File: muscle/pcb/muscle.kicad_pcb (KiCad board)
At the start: 4 copper layers, 135 x 50 mm, 166 parts, among them J1 B4B-XH-2(LF)(SN), J10 USB4115-03-C, J2 WAFER-SH1.0-3PWB, J4 WAFER-SH1.0-3PWB, J5 B4B-XH-2(LF)(SN), J8 B2B-XH-A(LF)(SN), J9 USB4115-03-C, Q1 AO3401A, Q10 BSS138W, Q2 AONR21321, Q3 WSD6070DN56, Q4 WSD6070DN56, Q5 BSS138W, Q6 WSD6070DN56, Q7 AONR21321, Q8 WSD6070DN56, Q9 AGM18N10AP, SW1 TS3425BA, SW2 TS3425BA, U1 TMC2209-LA, U10 TPS62933, U13 TLV75733PDBV, U14 DRV8701P, U2 TMC2209-LA, U3 RP2350A, U4 CYPD3177-24LQ, U5 LM5156, U6 W25Q128JVSS, Y1 ABM8-272-T3

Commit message: muscle: more TMC air
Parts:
- RV4: value I_{SINK_COARSE} -> I_{SNK_COARSE}
- moved RV4 0.50 mm to (111.0, 118.2)
- moved C32 0.35 mm to (141.4, 117.2)
- moved C23 0.23 mm to (77.3, 103.4)
- moved RV6 0.10 mm to (107.7, 100.9)
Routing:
- net /Y_DIR: track 130.5 -> 126.5 mm
- net /X_DIR: track 84.0 -> 81.0 mm
- net +3V3: track 150.3 -> 152.4 mm, vias 4 -> 6
- net /STEP_UART: track 117.8 -> 119.7 mm
- net /X_STEP: track 77.7 -> 79.5 mm
- net GND: track 149.2 -> 150.9 mm
- net /PD_VDDD: track 28.8 -> 30.5 mm
- net /Y_STEP: track 120.8 -> 119.3 mm
- net Net-(U1-VREF): track 9.07 -> 10.5 mm
- net /~{DRV_EN}: track 132.1 -> 131.1 mm
- net /X_DIAG: track 76.2 -> 76.8 mm
- net /Y_DIAG: track 112.5 -> 111.9 mm
- net /ISNK_COARSE: track 5.91 -> 6.41 mm

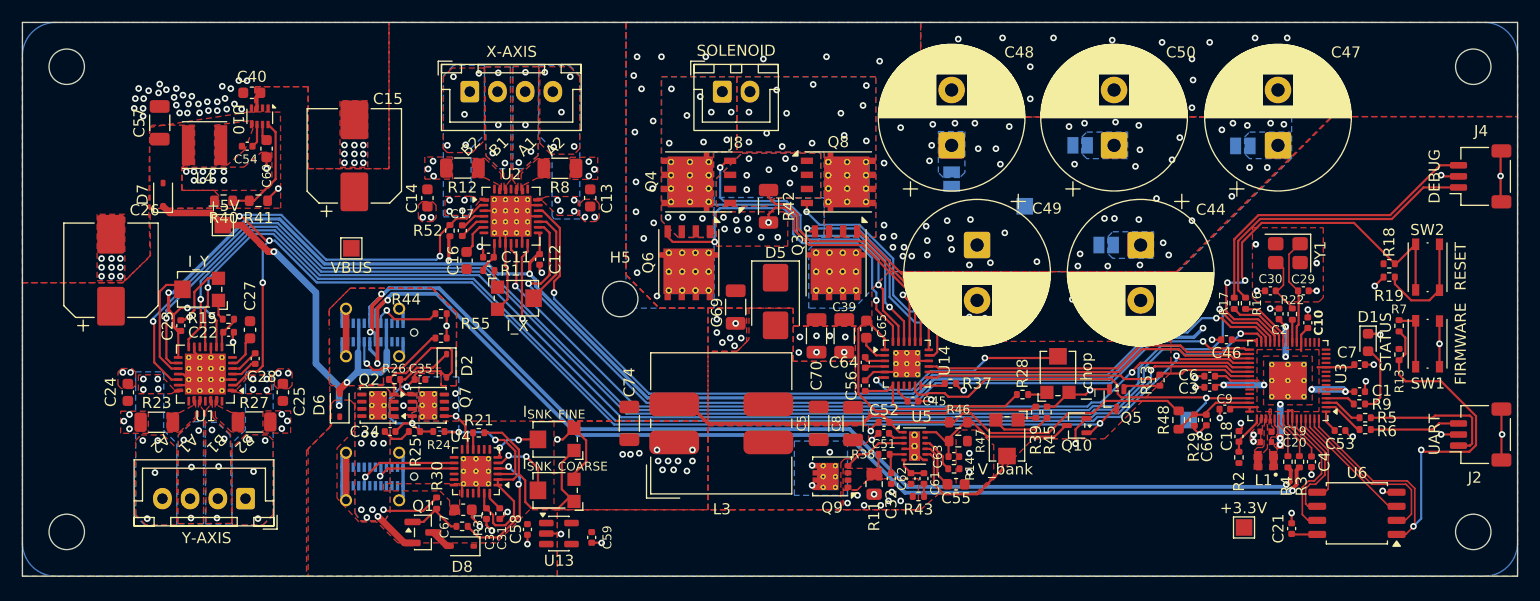
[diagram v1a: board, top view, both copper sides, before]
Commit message: muscle: tweak for easier USB-C flipping
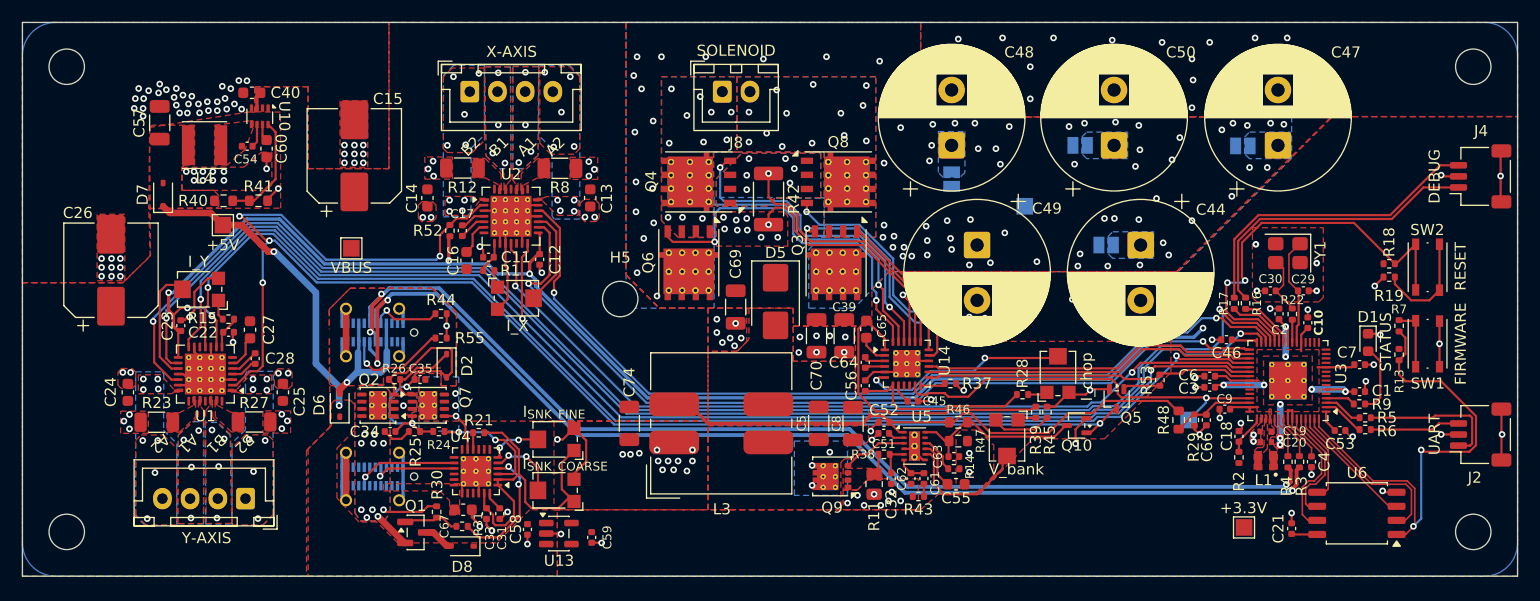
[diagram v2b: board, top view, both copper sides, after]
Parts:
- R42: footprint Resistor_SMD:R_1206_3216Metric -> Resistor_SMD:R_2010_5025Metric
- moved R30 0.80 mm to (100.4, 120.2)
- moved Q1 0.66 mm to (98.5, 122.0)
- moved R42 0.65 mm to (130.4, 92.0)
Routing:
- net Net-(U14-SP): track 23.6 -> 25.1 mm
- net VBUS0: track 12.2 -> 11.3 mm
- net Net-(D8-A): track 2.05 -> 2.71 mm

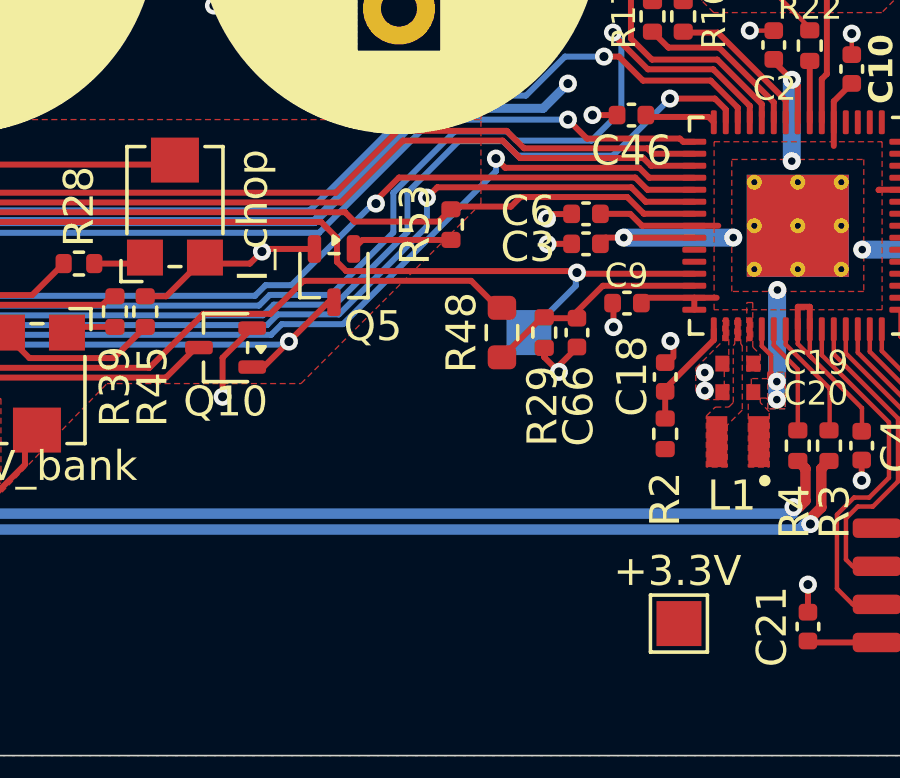
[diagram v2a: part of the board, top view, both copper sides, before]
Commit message: muscle: add current sense comparator
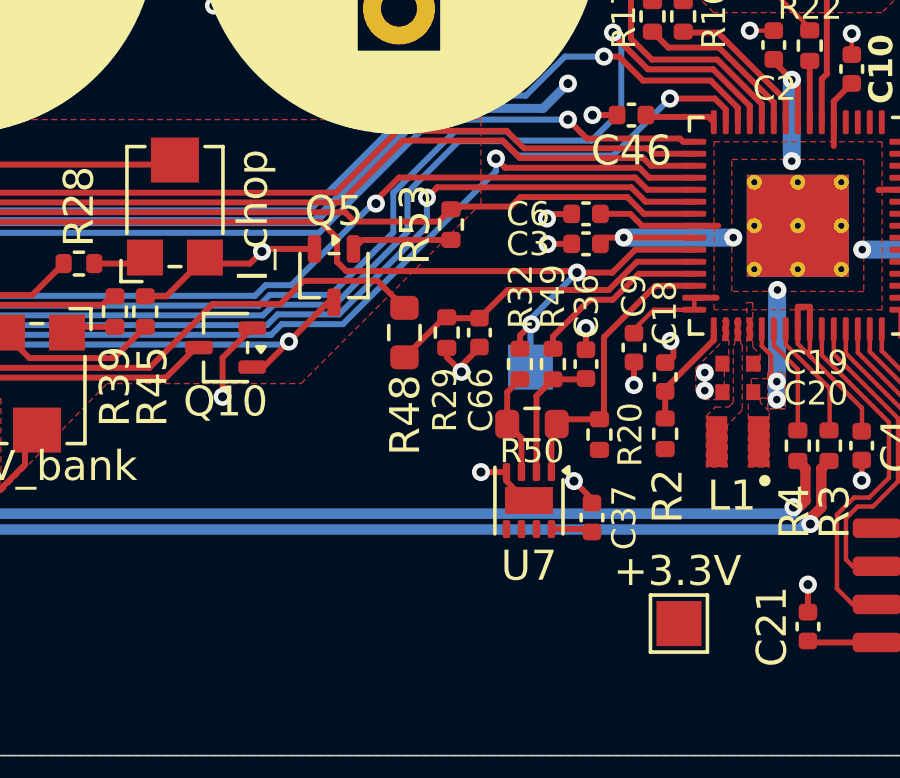
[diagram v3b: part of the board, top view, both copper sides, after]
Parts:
- added C36: 1u, Capacitor_SMD:C_0402_1005Metric, F.Cu at (170.2, 113.0)
- added C37: 1u, Capacitor_SMD:C_0402_1005Metric, F.Cu at (170.4, 118.1)
- added R20: 10k, Resistor_SMD:R_0402_1005Metric, F.Cu at (170.7, 115.3)
- added R32: 1k, Resistor_SMD:R_0402_1005Metric, F.Cu at (168.0, 113.0)
- added R49: 5.1k, Resistor_SMD:R_0402_1005Metric, F.Cu at (169.1, 113.0)
- added R50: 150k, Resistor_SMD:R_0603_1608Metric, F.Cu at (168.4, 115.0)
- added U7: LM393BIDSGR, Package_SON:Texas_DSG0008A_WSON-8-1EP_2x2mm_P0.5mm_EP0.9x1.6mm, F.Cu at (168.3, 117.5)
- moved C66 3.25 mm to (166.7, 111.9)
- moved R29 3.25 mm to (165.6, 111.9)
- moved R48 3.25 mm to (164.2, 111.9)
- moved C9 1.50 mm to (171.8, 112.4), turned to -90 degrees
- moved TP6 1.15 mm to (168.3, 113.0)
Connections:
- U3 pad 40: unconnected-(U3-GPIO26/ADC0-Pad40) -> /S_SENSE
- U3 pad 41: unconnected-(U3-GPIO27/ADC1-Pad41) -> /VBUS_SENSE
- U3 pad 42: /S_SENSE -> /S_SENSE_PWM
- U3 pad 43: /VBUS_SENSE -> /S_SENSE_COMP
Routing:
- net /S_SENSE_COMP: track 0.00 -> 9.68 mm
- net /S_SENSE_PWM: track 0.00 -> 5.99 mm
- net Net-(U7A--): track 0.00 -> 4.43 mm
- net GND: track 150.9 -> 154.8 mm, vias 225 -> 228
- net Net-(U7A-+): track 0.00 -> 3.46 mm
- net /VBUS_SENSE: track 7.44 -> 10.9 mm
- net VBUS: track 55.6 -> 52.4 mm
- net /S_SENSE: track 35.5 -> 38.0 mm, vias 1 -> 2
- net +3V3: track 152.4 -> 154.4 mm

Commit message: muscle: wip PCB changes for DRP
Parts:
- removed R41: 13k, Resistor_SMD:R_0603_1608Metric
- removed R44, R55: 5.1k, Resistor_SMD:R_0402_1005Metric
- added C38: 1u, Capacitor_SMD:C_0402_1005Metric, F.Cu at (100.8, 100.7)
- added C41: 1u, Capacitor_SMD:C_0402_1005Metric, F.Cu at (95.2, 95.5)
- added R10: 900k, Resistor_SMD:R_0402_1005Metric, F.Cu at (100.8, 104.7)
- added R33: 50k, Resistor_SMD:R_0402_1005Metric, F.Cu at (98.2, 99.6)
- added R34: 10k, Resistor_SMD:R_0402_1005Metric, F.Cu at (84.0, 92.1)
- added U8: TUSB320, Package_DFN_QFN:Texas_X2QFN-12_1.6x1.6mm_P0.4mm, F.Cu at (101.2, 102.7)
- added U9: TPS2041BDBV, Package_TO_SOT_SMD:SOT-23-5, F.Cu at (95.2, 98.1)
- R40: value 68k -> 56k
- moved TP3 19.6 mm to (109.1, 107.2)
- moved D6 12.1 mm to (92.1, 98.5), turned to -90 degrees
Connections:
- net /CC1 renamed /PWR_CC1
- net /CC2 renamed /PWR_CC2
- net Net-(D6-A) renamed /VBUS_DATA
- J10 pad A5: Net-(J10-CC1) -> /DATA_CC1
- J10 pad B5: Net-(J10-CC2) -> /DATA_CC2
- U3 pad 19: unconnected-(U3-GPIO15-Pad19) -> /USB_ROLE
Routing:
- net /USB_ROLE: track 0.00 -> 104.4 mm, vias 0 -> 2
- net /VBUS_DATA: track 13.8 -> 25.7 mm, vias 1 -> 2
- net /DATA_CC2: track 0.00 -> 11.6 mm, vias 0 -> 1
- net +5V: track 28.1 -> 38.3 mm
- net Net-(J10-CC2): track 9.67 -> 0.00 mm, vias 1 -> 0
- net +3V3: track 154.4 -> 161.4 mm, vias 6 -> 7
- net /DATA_CC1: track 0.00 -> 6.56 mm, vias 0 -> 1
- net Net-(J10-CC1): track 6.37 -> 0.00 mm, vias 1 -> 0
- net GND: track 154.8 -> 159.2 mm
- net Net-(U8-VBUS_DET): track 0.00 -> 1.24 mm
- net /~{DRV_EN}: track 131.1 -> 130.4 mm

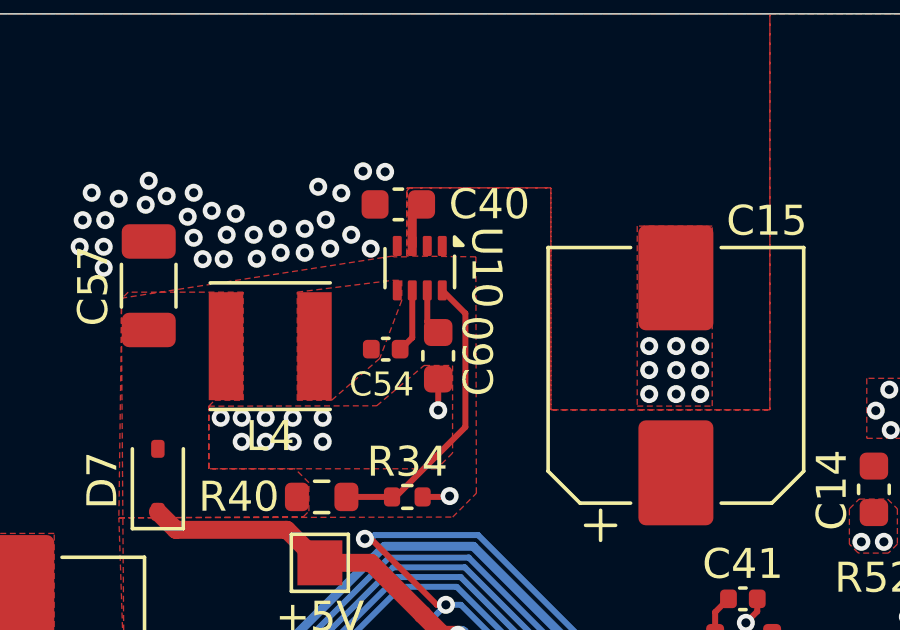
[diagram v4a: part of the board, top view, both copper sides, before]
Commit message: muscle: replace TPS62933 with the simpler and cheaper TPS563300
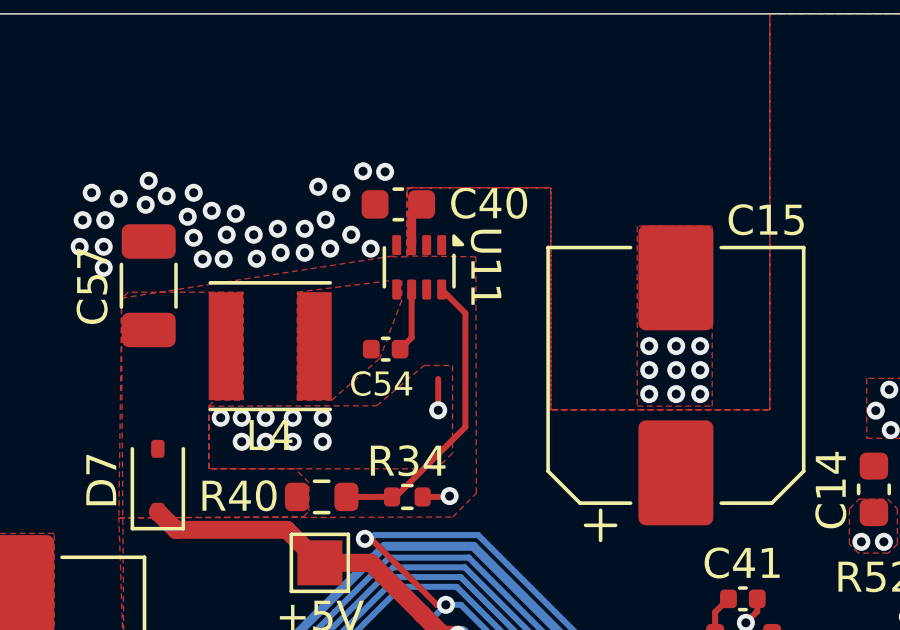
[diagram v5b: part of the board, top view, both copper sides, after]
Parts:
- removed C60: 33n, Capacitor_SMD:C_0603_1608Metric
- removed U10: TPS62933, Package_TO_SOT_SMD:SOT-583-8
- added U11: TPS563300, Package_TO_SOT_SMD:SOT-583-8, F.Cu at (84.4, 84.5)
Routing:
- net Net-(U10-SS): track 1.56 -> 0.00 mm
